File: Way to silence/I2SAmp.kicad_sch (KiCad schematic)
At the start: 9 parts, among them J2 Amplificator_Terminal

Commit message: [ADD] i2S Module placed
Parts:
- FB? (x2): footprint Way to silence:Inductor -> Way to silence:FB_0603; LCSC C2847468 -> C394474
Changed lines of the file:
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@@
       (effects (font (size 1.27 1.27)))
     )
-    (property "Footprint" "Way to silence:Inductor" (at 106.68 46.228 0)
+    (property "Footprint" "Way to silence:FB_0603" (at 106.68 46.228 0)
       (effects (font (size 1.27 1.27)) hide)
     )
@@
       (effects (font (size 1.27 1.27)) hide)
     )
-    (property "LCSC" "C2847468" (at 106.68 44.45 0)
+    (property "LCSC" "C394474" (at 106.68 44.45 0)
       (effects (font (size 1.27 1.27)) hide)
     )
@@
     )
   )
-  (symbol (lib_name "FerriteBead_1") (lib_id "Way to silence:FerriteBead") (at 106.68 57.15 0) (unit 1)
+  (symbol (lib_id "Way to silence:FerriteBead") (at 106.68 57.15 0) (unit 1)
     (in_bom yes) (on_board yes) (dnp no)
     (property "Reference" "FB?" (at 106.6292 49.53 0)
@@
       (effects (font (size 1.27 1.27)))
     )
-    (property "Footprint" "Way to silence:Inductor" (at 106.68 58.928 0)
+    (property "Footprint" "Way to silence:FB_0603" (at 106.68 58.928 0)
       (effects (font (size 1.27 1.27)) hide)
     )
@@
       (effects (font (size 1.27 1.27)) hide)
     )
-    (property "LCSC" "C2847468" (at 106.68 48.26 0)
+    (property "LCSC" "C394474" (at 106.68 48.26 0)
       (effects (font (size 1.27 1.27)) hide)
     )

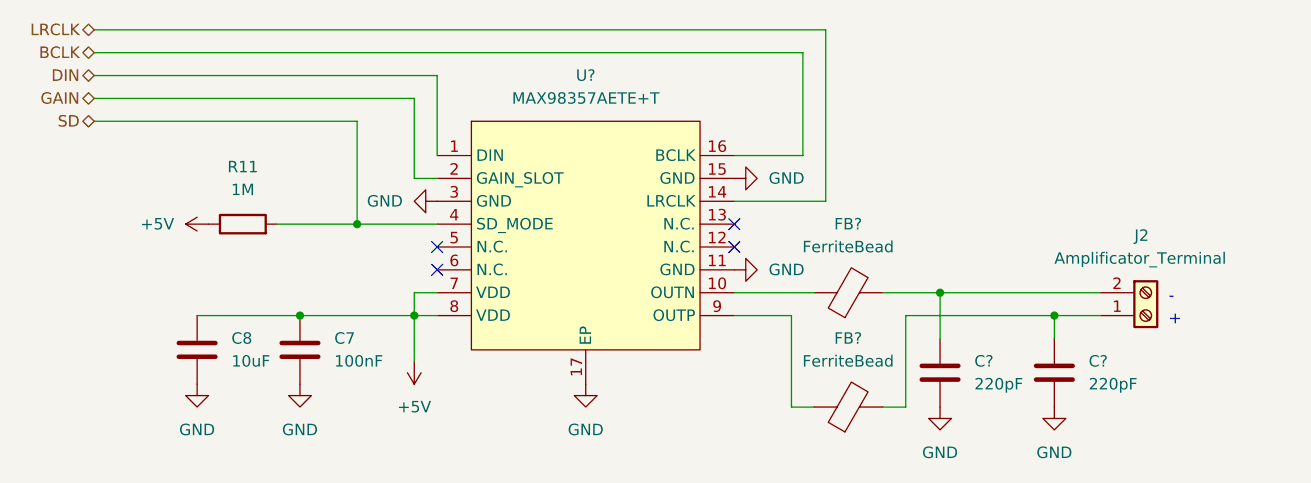
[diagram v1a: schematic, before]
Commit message: [FIX] DRC and replacing button
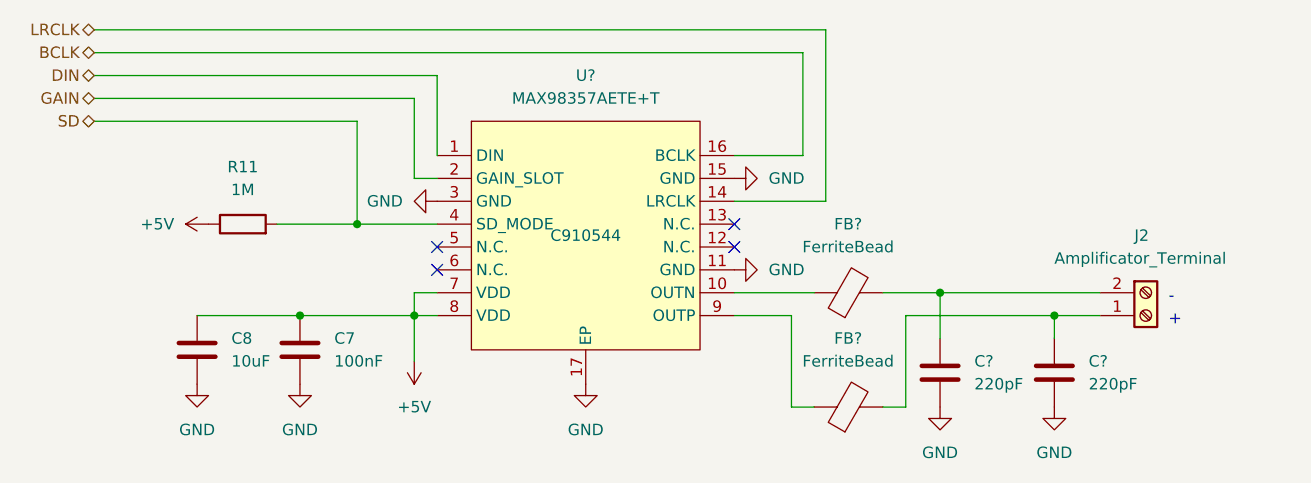
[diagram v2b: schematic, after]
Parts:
- U?: LSCS (none) -> C910544
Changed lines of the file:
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@@
       (effects (font (size 1.27 1.27)) hide)
+    )
+    (property "LSCS" "C910544" (at 77.47 38.1 0)
+      (effects (font (size 1.27 1.27)))
     )
     (pin "1")

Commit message: [ADD] Shematics files settings
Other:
- title: (none) -> I2S Amplifier
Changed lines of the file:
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@@
 (kicad_sch (version 20230121) (generator eeschema)
-  (paper "A4")
+  (paper "A5")
+  (title_block
+    (title "I2S Amplifier")
+    (date "2023-10-10")
+    (rev "1.0")
+  )
   (junction (at 45.72 46.99) (diameter 0) (color 0 0 0 0)
   )

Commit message: [FIX] LCSC Parts property
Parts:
- R11: LCSC (none) -> C22935; LSCS C22935 -> (none)
- U?: LCSC (none) -> C910544; LSCS C910544 -> (none)
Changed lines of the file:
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@@
       (effects (font (size 1.27 1.27)) hide)
     )
-    (property "LSCS" "C22935" (at 39.37 36.83 0)
+    (property "LCSC" "C22935" (at 39.37 36.83 0)
       (effects (font (size 1.27 1.27)) hide)
     )
@@
       (effects (font (size 1.27 1.27)) hide)
     )
-    (property "LSCS" "C910544" (at 77.47 38.1 0)
+    (property "LCSC" "C910544" (at 77.47 38.1 0)
       (effects (font (size 1.27 1.27)))
     )

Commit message: [ADD] Terminals Rotations
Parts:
- J2: JLCPCB Rotation Offset (none) -> 180
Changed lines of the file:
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@@
+      (effects (font (size 1.27 1.27)) hide)
+    )
+    (property "JLCPCB Rotation Offset" "180" (at 139.7 39.37 0)
       (effects (font (size 1.27 1.27)) hide)
     )

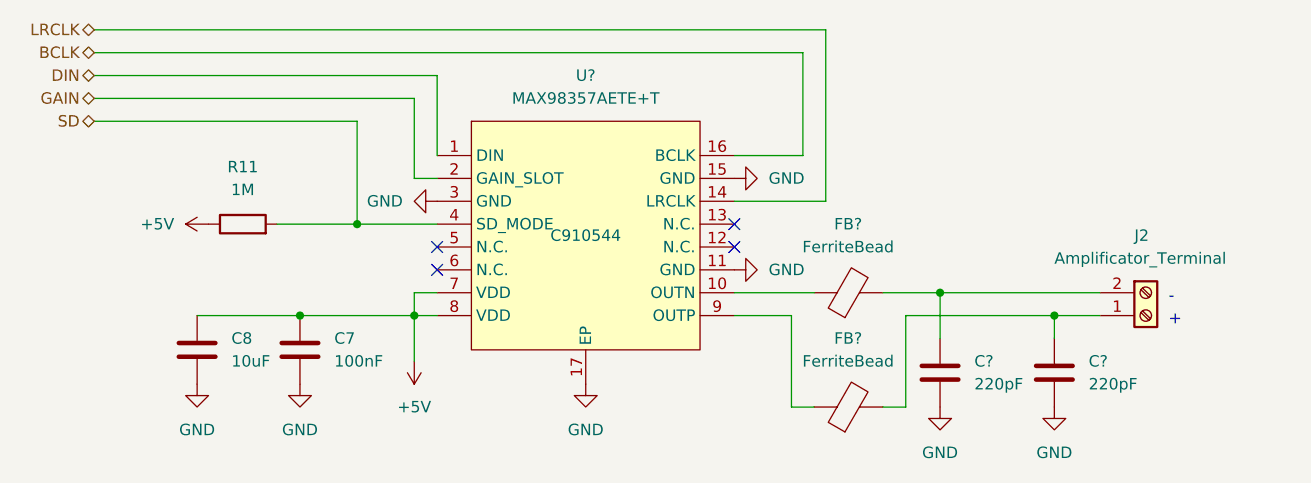
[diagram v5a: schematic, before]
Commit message: [ADD] Better 3D models
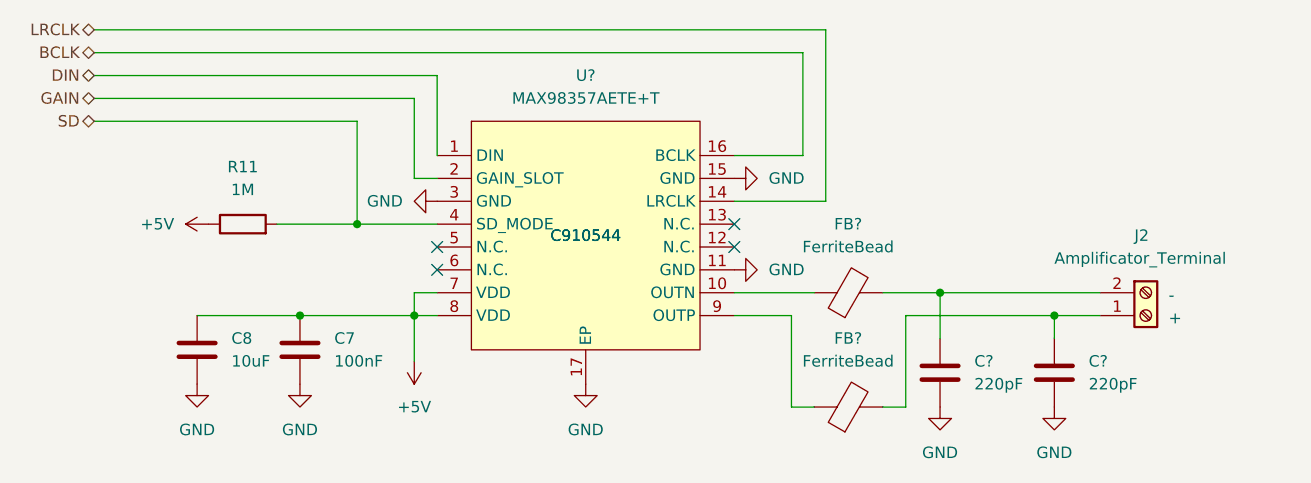
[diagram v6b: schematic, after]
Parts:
- U?: LSCS (none) -> C910544
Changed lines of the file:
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@@
+      (effects (font (size 1.27 1.27)))
+    )
+    (property "LSCS" "C910544" (at 77.47 38.1 0)
       (effects (font (size 1.27 1.27)))
     )
